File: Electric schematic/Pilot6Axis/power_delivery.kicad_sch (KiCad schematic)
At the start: 47 parts, among them IC3 BQ25792RQMR, IC4 TPS25751SRSMR, Q2 AO3400A, Q4 AO3400A

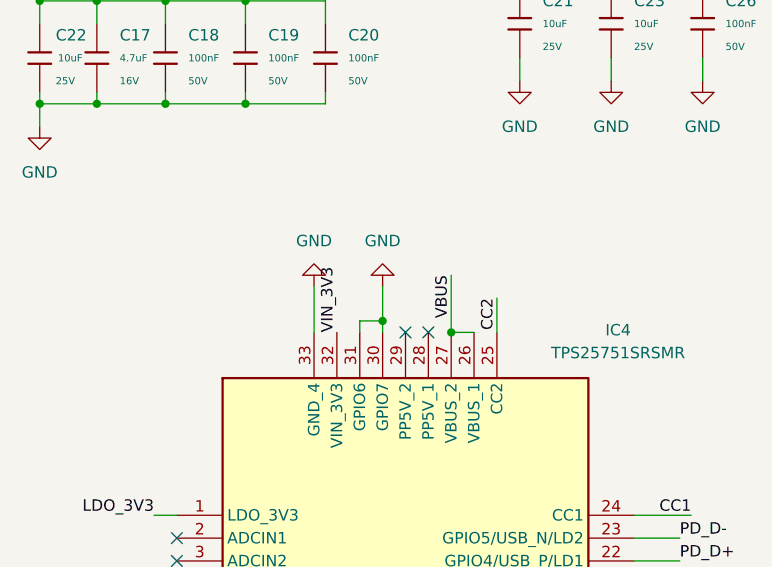
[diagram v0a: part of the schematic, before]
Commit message: [pd] added 5V to PD
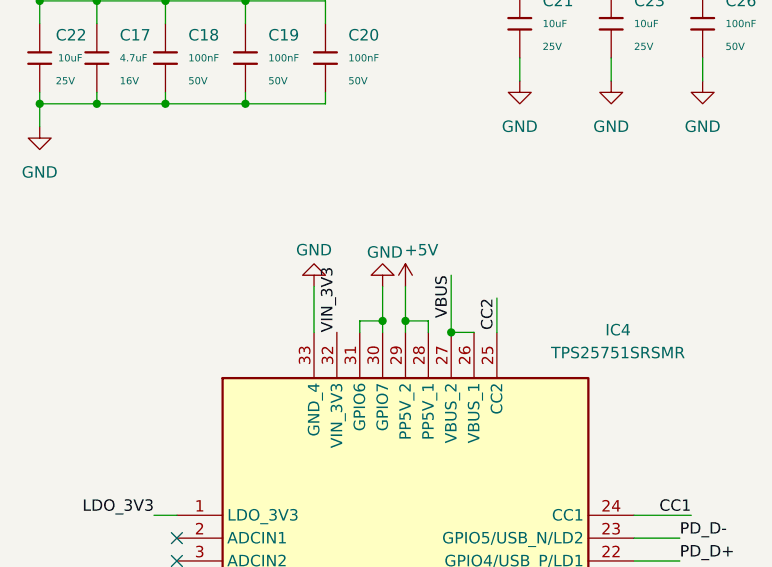
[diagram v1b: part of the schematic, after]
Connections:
- net +5V: now reaches IC4.28 (PP5V_1)
- net +5V: now also IC4.29 (PP5V_2)
- no-connect marks 9 -> 7
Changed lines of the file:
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@@
 	)
 	(junction
+		(at 57.15 60.96)
+		(diameter 0)
+		(color 0 0 0 0)
+	)
+	(junction
 		(at 260.35 107.95)
 		(diameter 0)
@@
 	)
 	(no_connect
-		(at 57.15 62.23)
-	)
-	(no_connect
 		(at 31.75 85.09)
 	)
@@
 	)
 	(no_connect
-		(at 59.69 62.23)
-	)
-	(no_connect
 		(at 82.55 100.33)
 	)
@@
 	(wire
 		(pts
+			(xy 57.15 57.15) (xy 57.15 60.96)
+		)
+		(stroke
+			(width 0)
+			(type default)
+		)
+	)
+	(wire
+		(pts
 			(xy 191.77 73.66) (xy 191.77 71.12)
 		)
@@
 	(wire
 		(pts
+			(xy 59.69 62.23) (xy 59.69 60.96)
+		)
+		(stroke
+			(width 0)
+			(type default)
+		)
+	)
+	(wire
+		(pts
 			(xy 182.88 91.44) (xy 187.96 91.44)
 		)
@@
 	(wire
 		(pts
+			(xy 57.15 60.96) (xy 59.69 60.96)
+		)
+		(stroke
+			(width 0)
+			(type default)
+		)
+	)
+	(wire
+		(pts
 			(xy 181.61 25.4) (xy 181.61 27.94)
 		)
@@
 	(wire
 		(pts
+			(xy 57.15 60.96) (xy 57.15 62.23)
+		)
+		(stroke
+			(width 0)
+			(type default)
+		)
+	)
+	(wire
+		(pts
 			(xy 227.33 68.58) (xy 232.41 68.58)
 		)
@@
 		(on_board yes)
 		(dnp no)
-		(fields_autoplaced yes)
 		(property "Reference" "#PWR023"
 			(at 46.99 50.8 0)
@@
 		)
 		(property "Value" "GND"
-			(at 46.99 52.07 0)
+			(at 46.99 53.086 0)
 			(effects
 				(font
@@
 	)
 	(symbol
+		(lib_id "power:+5V")
+		(at 57.15 57.15 0)
+		(unit 1)
+		(exclude_from_sim no)
+		(in_bom yes)
+		(on_board yes)
+		(dnp no)
+		(property "Reference" "#PWR045"
+			(at 57.15 60.96 0)
+			(effects
+				(font
+					(size 1.27 1.27)
+				)
+				(hide yes)
+			)
+		)
+		(property "Value" "+5V"
+			(at 58.928 53.086 0)
+			(effects
+				(font
+					(size 1.27 1.27)
+				)
+			)
+		)
+		(property "Footprint" ""
+			(at 57.15 57.15 0)
+			(effects
+				(font
+					(size 1.27 1.27)
+				)
+				(hide yes)
+			)
+		)
+		(property "Datasheet" ""
+			(at 57.15 57.15 0)
+			(effects
+				(font
+					(size 1.27 1.27)
+				)
+				(hide yes)
+			)
+		)
+		(property "Description" "Power symbol creates a global label with name \"+5V\""
+			(at 57.15 57.15 0)
+			(effects
+				(font
+					(size 1.27 1.27)
+				)
+				(hide yes)
+			)
+		)
+		(pin "1"
+		)
+		(instances
+			(project ""
+				(path "/085b8362-a5df-4186-a09b-4280628dd4a5/53200cc9-36ae-481d-b1ee-e4ac6bfba1fc"
+					(reference "#PWR045")
+					(unit 1)
+				)
+			)
+		)
+	)
+	(symbol
 		(lib_id "power:GND")
 		(at 54.61 57.15 180)
@@
 		(on_board yes)
 		(dnp no)
-		(fields_autoplaced yes)
 		(property "Reference" "#PWR055"
 			(at 54.61 50.8 0)
@@
 		)
 		(property "Value" "GND"
-			(at 54.61 52.07 0)
+			(at 54.864 53.34 0)
 			(effects
 				(font

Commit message: fixed leyout
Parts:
- removed R17, R18: 22Ω, PCM_JLCPCB:R_0603, symbol PCM_JLCPCB-Resistors:0603,22Ω
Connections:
- net PD_D+: no longer names the net of IC4.22 (GPIO4/USB_P/LD1)
- net PD_D-: no longer names the net of IC4.23 (GPIO5/USB_N/LD2)
- no-connect marks 7 -> 9
